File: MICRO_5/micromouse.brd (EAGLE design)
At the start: 100 x 80 mm, 34 parts

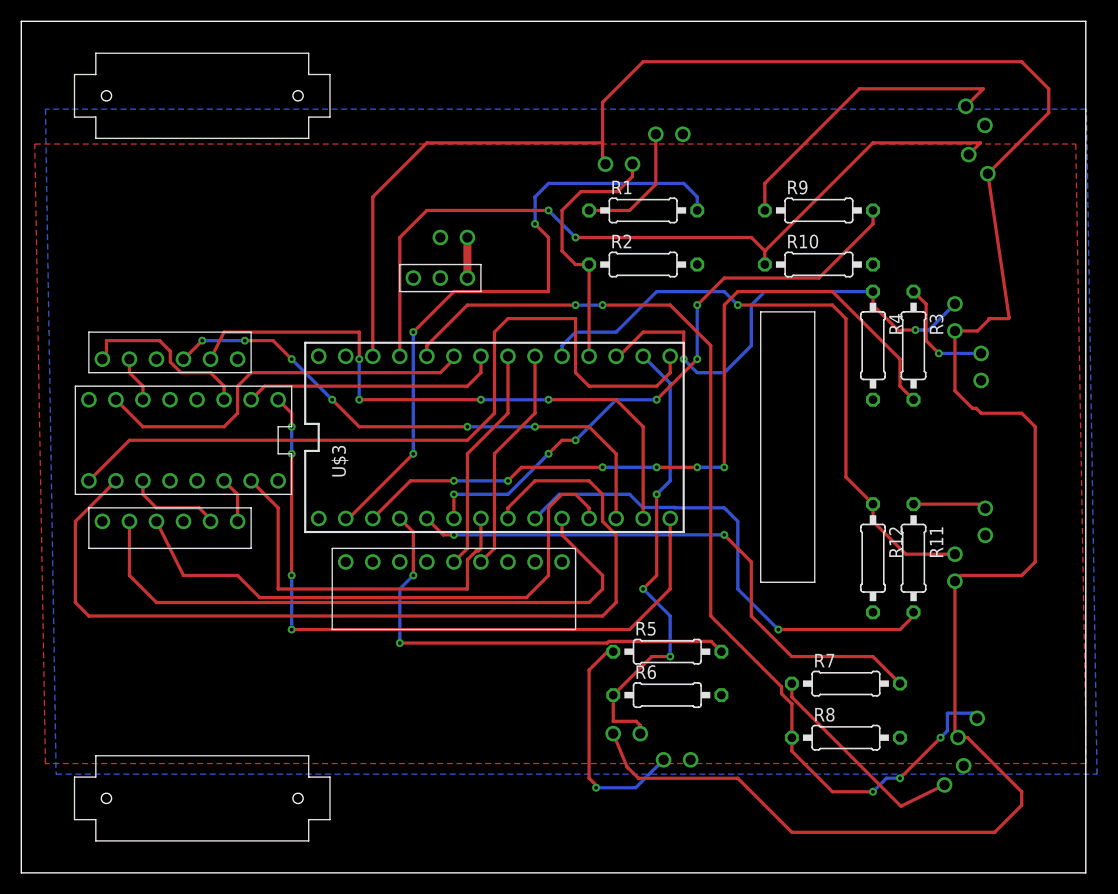
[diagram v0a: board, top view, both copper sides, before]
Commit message: added more space in between led's
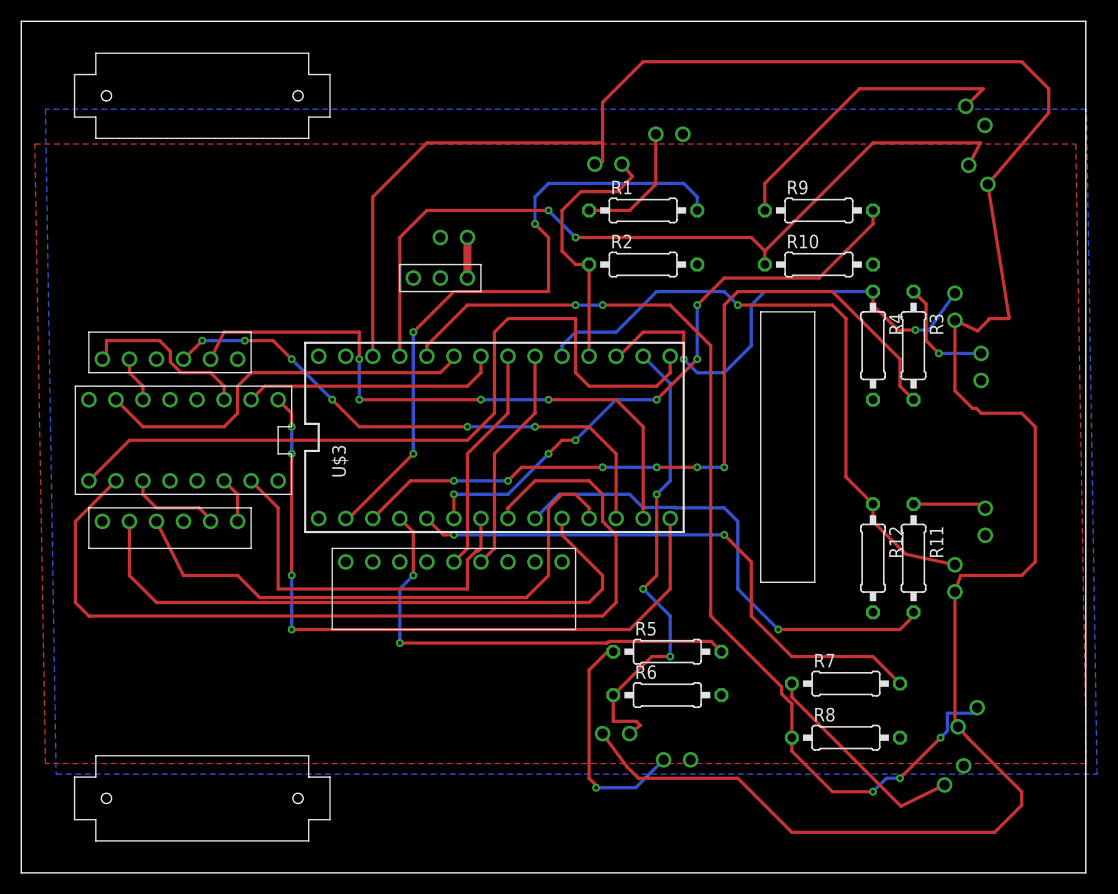
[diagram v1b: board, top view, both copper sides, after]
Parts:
- moved U$12 1.00 mm to (87.7, 53.2)
- moved U$15 1.00 mm to (88.9, 14.6)
- moved U$17 1.00 mm to (89.9, 65.6)
- moved U$23 1.00 mm to (87.7, 27.7)
- moved U$5 1.00 mm to (55.1, 66.6)
- moved U$8 1.00 mm to (55.9, 13.1)
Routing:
- net 3.3V_VCC: track 222.6 -> 223.8 mm
- net N$12: track 75.4 -> 76.2 mm
- net N$24: track 44.6 -> 45.4 mm
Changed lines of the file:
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@@
 <setting verticaltext="up"/>
 </settings>
-<grid distance="1" unitdist="mm" unit="mm" style="lines" multiple="1" display="yes" altdistance="5" altunitdist="mil" altunit="mil"/>
+<grid distance="50" unitdist="mil" unit="mil" style="lines" multiple="1" display="yes" altdistance="5" altunitdist="mil" altunit="mil"/>
 <layers>
 <layer number="1" name="Top" color="4" fill="1" visible="yes" active="yes"/>
@@
 <element name="U$10" library="VOLTAGE_REGULATOR" package="VOLTAGE_REGULATOR" value="VOLTAGE_REGULATOR" x="39.37" y="55.88"/>
 <element name="U$11" library="Battery_input" package="BATTERY_INPUT" value="BATTERY_INPUT" x="40.64" y="59.69" rot="R180"/>
-<element name="U$12" library="IR_RECIEVER" package="IR_RECIEVER" value="IR_RECIEVER" x="87.71" y="52.18" rot="R90"/>
+<element name="U$12" library="IR_RECIEVER" package="IR_RECIEVER" value="IR_RECIEVER" x="87.71" y="53.18" rot="R90"/>
 <element name="U$13" library="IMU" package="IMU" value="IMU" x="45.72" y="27.94" rot="R270"/>
 <element name="U$14" library="IR_EMITTER" package="IR_EMITTER" value="IR_EMITTER" x="87.63" y="9.16" rot="R45"/>
-<element name="U$15" library="IR_RECIEVER" package="IR_RECIEVER" value="IR_RECIEVER" x="88.9" y="13.62" rot="R45"/>
+<element name="U$15" library="IR_RECIEVER" package="IR_RECIEVER" value="IR_RECIEVER" x="88.9" y="14.62" rot="R45"/>
 <element name="U$16" library="IR_EMITTER" package="IR_EMITTER" value="IR_EMITTER" x="89.63" y="71.12" rot="R315"/>
-<element name="U$17" library="IR_RECIEVER" package="IR_RECIEVER" value="IR_RECIEVER" x="89.9" y="66.58" rot="R135"/>
+<element name="U$17" library="IR_RECIEVER" package="IR_RECIEVER" value="IR_RECIEVER" x="89.9" y="65.58" rot="R135"/>
 <element name="U$2" library="MOTOR_ENCODER" package="MOTOR_ENCODER" value="MOTOR_ENCODER" x="11.43" y="34.29" rot="R90"/>
 <element name="U$22" library="IR_EMITTER" package="IR_EMITTER" value="IR_EMITTER" x="90.56" y="32.98" rot="R270"/>
-<element name="U$23" library="IR_RECIEVER" package="IR_RECIEVER" value="IR_RECIEVER" x="87.71" y="28.67" rot="R90"/>
+<element name="U$23" library="IR_RECIEVER" package="IR_RECIEVER" value="IR_RECIEVER" x="87.71" y="27.67" rot="R90"/>
 <element name="U$3" library="Teensy_3_and_LC_Series_Boards_v1.4" package="TEENSY_3.0-3.2&amp;LC_DIL" value="TEENSY_3.1-3.2_DIL" x="44.45" y="40.91" rot="R90"/>
 <element name="U$4" library="motor_driver" package="MOTOR_DRIVER" value="MOTOR_DRIVER" x="17.78" y="40.64" rot="R270"/>
-<element name="U$5" library="IR_RECIEVER" package="IR_RECIEVER" value="IR_RECIEVER" x="56.15" y="66.58"/>
+<element name="U$5" library="IR_RECIEVER" package="IR_RECIEVER" value="IR_RECIEVER" x="55.15" y="66.58"/>
 <element name="U$6" library="IR_EMITTER" package="IR_EMITTER" value="IR_EMITTER" x="90.17" y="47.53" rot="R270"/>
 <element name="U$7" library="IR_EMITTER" package="IR_EMITTER" value="IR_EMITTER" x="61.61" y="10.62"/>
-<element name="U$8" library="IR_RECIEVER" package="IR_RECIEVER" value="IR_RECIEVER" x="56.88" y="13.08"/>
+<element name="U$8" library="IR_RECIEVER" package="IR_RECIEVER" value="IR_RECIEVER" x="55.88" y="13.08"/>
 <element name="U$9" library="IR_EMITTER" package="IR_EMITTER" value="IR_EMITTER" x="60.88" y="69.39"/>
 <element name="U$18" library="MOTOR_BRACKET" package="MOTOR_BRACKET" value="MOTOR_BRACKET" x="17" y="7"/>
@@
 <wire x1="60.96" y1="36.83" x2="60.96" y2="45.99" width="0.3048" layer="16"/>
 <wire x1="55.61" y1="14.24" x2="57.76" y2="14.24" width="0.3048" layer="1"/>
-<wire x1="58.15" y1="13.85" x2="58.15" y2="13.08" width="0.3048" layer="1"/>
+<wire x1="58.15" y1="13.85" x2="57.15" y2="13.08" width="0.3048" layer="1"/>
 <wire x1="57.76" y1="14.24" x2="58.15" y2="13.85" width="0.3048" layer="1"/>
 </signal>
@@
 <via x="84" y="51" extent="1-16" drill="0.35"/>
 <wire x1="84" y1="51" x2="85.26" y2="51" width="0.3048" layer="16"/>
-<wire x1="85.26" y1="51" x2="87.71" y2="53.45" width="0.3048" layer="16"/>
+<wire x1="85.26" y1="51" x2="87.71" y2="54.45" width="0.3048" layer="16"/>
 </signal>
 <signal name="N$28">
@@
 <wire x1="53.34" y1="57.15" x2="53.34" y2="48.53" width="0.3048" layer="1"/>
 <wire x1="50.8" y1="62.23" x2="52.57" y2="64" width="0.3048" layer="1"/>
-<wire x1="57.42" y1="65.42" x2="57.42" y2="66.58" width="0.3048" layer="1"/>
+<wire x1="57.42" y1="65.42" x2="56.42" y2="66.58" width="0.3048" layer="1"/>
 <wire x1="52.57" y1="64" x2="56" y2="64" width="0.3048" layer="1"/>
 <wire x1="56" y1="64" x2="57.42" y2="65.42" width="0.3048" layer="1"/>
@@
 <via x="86.36" y="12.7" extent="1-16" drill="0.35"/>
 <wire x1="86.36" y1="12.7" x2="87" y2="13.34" width="0.3048" layer="16"/>
+<wire x1="87" y1="15" x2="89.31605" y2="15" width="0.3048" layer="16"/>
+<wire x1="89.31605" y1="15" x2="89.798025" y2="15.518025" width="0.3048" layer="16"/>
+<wire x1="82.55" y1="8.89" x2="86.36" y2="12.7" width="0.3048" layer="1"/>
 <wire x1="87" y1="13.34" x2="87" y2="15" width="0.3048" layer="16"/>
-<wire x1="87" y1="15" x2="89.31605" y2="15" width="0.3048" layer="16"/>
-<wire x1="89.31605" y1="15" x2="89.798025" y2="14.518025" width="0.3048" layer="16"/>
-<wire x1="82.55" y1="8.89" x2="86.36" y2="12.7" width="0.3048" layer="1"/>
 </signal>
 <signal name="N$12">
@@
 <contactref element="R10" pad="1"/>
 <contactref element="U$3" pad="23/A9"/>
-<wire x1="89.001971875" y1="67.478025" x2="90.103946875" y2="68.58" width="0.3048" layer="1"/>
+<wire x1="89.001971875" y1="66.478025" x2="90.103946875" y2="68.58" width="0.3048" layer="1"/>
 <wire x1="90.103946875" y1="68.58" x2="80.01" y2="68.58" width="0.3048" layer="1"/>
 <wire x1="80.01" y1="68.58" x2="69.85" y2="58.42" width="0.3048" layer="1"/>
@@
 <contactref element="R12" pad="1"/>
 <contactref element="U$3" pad="17/A3"/>
-<wire x1="87.71" y1="29.94" x2="83.09" y2="29.94" width="0.3048" layer="1"/>
+<wire x1="87.71" y1="28.94" x2="83.09" y2="29.94" width="0.3048" layer="1"/>
 <wire x1="80.01" y1="33.02" x2="80.01" y2="34.64" width="0.3048" layer="1"/>
 <wire x1="83.09" y1="29.94" x2="80.01" y2="33.02" width="0.3048" layer="1"/>
@@
 <wire x1="91" y1="52.07" x2="92.71" y2="52.07" width="0.3048" layer="1"/>
 <wire x1="92.71" y1="52.07" x2="92.798025" y2="52.158025" width="0.3048" layer="1"/>
-<wire x1="92.798025" y1="52.158025" x2="90.798025" y2="65.681971875" width="0.3048" layer="1"/>
+<wire x1="92.798025" y1="52.158025" x2="90.798025" y2="64.681971875" width="0.3048" layer="1"/>
 <wire x1="54.61" y1="68.58" x2="38.1" y2="68.58" width="0.3048" layer="1"/>
 <wire x1="33.02" y1="63.5" x2="33.02" y2="48.53" width="0.3048" layer="1"/>
 <wire x1="38.1" y1="68.58" x2="33.02" y2="63.5" width="0.3048" layer="1"/>
-<wire x1="55.61" y1="13.08" x2="56.90453125" y2="9.960384375" width="0.3048" layer="1"/>
+<wire x1="54.61" y1="13.08" x2="56.90453125" y2="9.960384375" width="0.3048" layer="1"/>
 <wire x1="72.39" y1="3.81" x2="91.44" y2="3.81" width="0.3048" layer="1"/>
 <wire x1="91.44" y1="3.81" x2="93.98" y2="6.35" width="0.3048" layer="1"/>
@@
 <wire x1="72.39" y1="3.81" x2="67.31" y2="8.89" width="0.3048" layer="1"/>
 <wire x1="93.98" y1="7.62" x2="88.878028125" y2="12.721971875" width="0.3048" layer="1"/>
-<wire x1="90.798025" y1="65.681971875" x2="96.52" y2="71.403946875" width="0.3048" layer="1"/>
+<wire x1="90.798025" y1="64.681971875" x2="96.52" y2="71.403946875" width="0.3048" layer="1"/>
 <wire x1="96.52" y1="73.66" x2="93.98" y2="76.2" width="0.3048" layer="1"/>
 <wire x1="58.42" y1="76.2" x2="54.61" y2="72.39" width="0.3048" layer="1"/>
@@
 <wire x1="93.98" y1="76.2" x2="58.42" y2="76.2" width="0.3048" layer="1"/>
 <wire x1="54.61" y1="68.58" x2="54.61" y2="66.85" width="0.3048" layer="1"/>
-<wire x1="54.61" y1="66.85" x2="54.88" y2="66.58" width="0.3048" layer="1"/>
-<wire x1="87.71" y1="50.91" x2="89.84" y2="50.91" width="0.3048" layer="1"/>
+<wire x1="54.61" y1="66.85" x2="53.88" y2="66.58" width="0.3048" layer="1"/>
+<wire x1="87.71" y1="51.91" x2="89.84" y2="50.91" width="0.3048" layer="1"/>
 <wire x1="89.84" y1="50.91" x2="91" y2="52.07" width="0.3048" layer="1"/>
 <wire x1="89.71" y1="43.64" x2="89.36" y2="43.64" width="0.3048" layer="1"/>
-<wire x1="87.71" y1="45.29" x2="87.71" y2="50.91" width="0.3048" layer="1"/>
+<wire x1="87.71" y1="45.29" x2="87.71" y2="51.91" width="0.3048" layer="1"/>
 <wire x1="89.36" y1="43.64" x2="87.71" y2="45.29" width="0.3048" layer="1"/>
-<wire x1="88.878028125" y1="12.721971875" x2="88.001971875" y2="12.721971875" width="0.3048" layer="1"/>
-<wire x1="88.25" y1="27.94" x2="87.71" y2="27.4" width="0.3048" layer="1"/>
-<wire x1="87.71" y1="27.4" x2="87.71" y2="13.01394375" width="0.3048" layer="1"/>
-<wire x1="87.71" y1="13.01394375" x2="88.001971875" y2="12.721971875" width="0.3048" layer="1"/>
-<wire x1="56.90453125" y1="9.960384375" x2="56.932459375" y2="9.93245625" width="0.3048" layer="1"/>
-<wire x1="56.932459375" y1="9.93245625" x2="57.0286" y2="9.836315625" width="0.3048" layer="1"/>
+<wire x1="88.878028125" y1="12.721971875" x2="88.001971875" y2="13.721971875" width="0.3048" layer="1"/>
+<wire x1="88.25" y1="27.94" x2="87.71" y2="26.4" width="0.3048" layer="1"/>
 <wire x1="67.31" y1="8.89" x2="57.974915625" y2="8.89" width="0.3048" layer="1"/>
-<wire x1="57.974915625" y1="8.89" x2="57.0286" y2="9.836315625" width="0.3048" layer="1"/>
+<wire x1="57.974915625" y1="8.89" x2="56.90453125" y2="9.960384375" width="0.3048" layer="1"/>
+<wire x1="88.001971875" y1="13.721971875" x2="87.71" y2="14.01394375" width="0.3048" layer="1"/>
+<wire x1="87.71" y1="14.01394375" x2="87.71" y2="26.4" width="0.3048" layer="1"/>
 </signal>
 </signals>
